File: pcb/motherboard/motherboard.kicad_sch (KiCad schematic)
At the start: 47 parts, among them J10 M20-7820646, J11 M20-7820646, J12 M20-7820646, J13 M20-7820646, J14 M20-7820646, J15 M20-7820646, J16 M20-7820646, J17 Terminal 1, J18 Terminal 2, J3 UART_USB, J4 I2C_HEADER, J6 SPI_TEST, J7 M20-7820646, J8 M20-7820646, J9 M20-7820646, SW2 GEN_MAZE, SW3 TOGGLE_MAZE, SW4 SOLVE_MAZE, U2 CH340C, U6 PCA9306D

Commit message: finished initial PCB layout for motherboard
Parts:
- removed H2: MountingHole, MountingHole:MountingHole_4.3mm_M4, symbol Mechanical:MountingHole
- removed J10, J12, J14, J16, J8: M20-7820646, KiCad:HDRV6W70P0X254_1X6_1564X250X850P, symbol KiCad:M20-7820646
- added C28, C29, C30, C31, C32: 220uF, Capacitor_SMD:CP_Elec_6.3x5.4, symbol Device:C_Polarized_Small_US
- added J19, J20, J21, J22, J23: Terminal Block, TerminalBlock_Phoenix:TerminalBlock_Phoenix_MKDS-1,5-3-5.08_1x03_P5.08mm_Horizontal, symbol Connector:Screw_Terminal_01x03
- added TP8: GND, TestPoint:TestPoint_Pad_2.0x2.0mm, symbol Connector:TestPoint
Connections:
- net +3V3: now also J19.2 (Pin_2), J20.2 (Pin_2), J21.2 (Pin_2), J22.2 (Pin_2), J23.2 (Pin_2)
- net +5V5: now also C28.1, C29.1, C30.1, C31.1, C32.1, J19.1 (Pin_1), J20.1 (Pin_1), J21.1 (Pin_1), J22.1 (Pin_1), J23.1 (Pin_1)
- net GND: now also C28.2, C29.2, C30.2, C31.2, C32.2, J19.3 (Pin_3), J20.3 (Pin_3), J21.3 (Pin_3), J22.3 (Pin_3), J23.3 (Pin_3), TP8.1

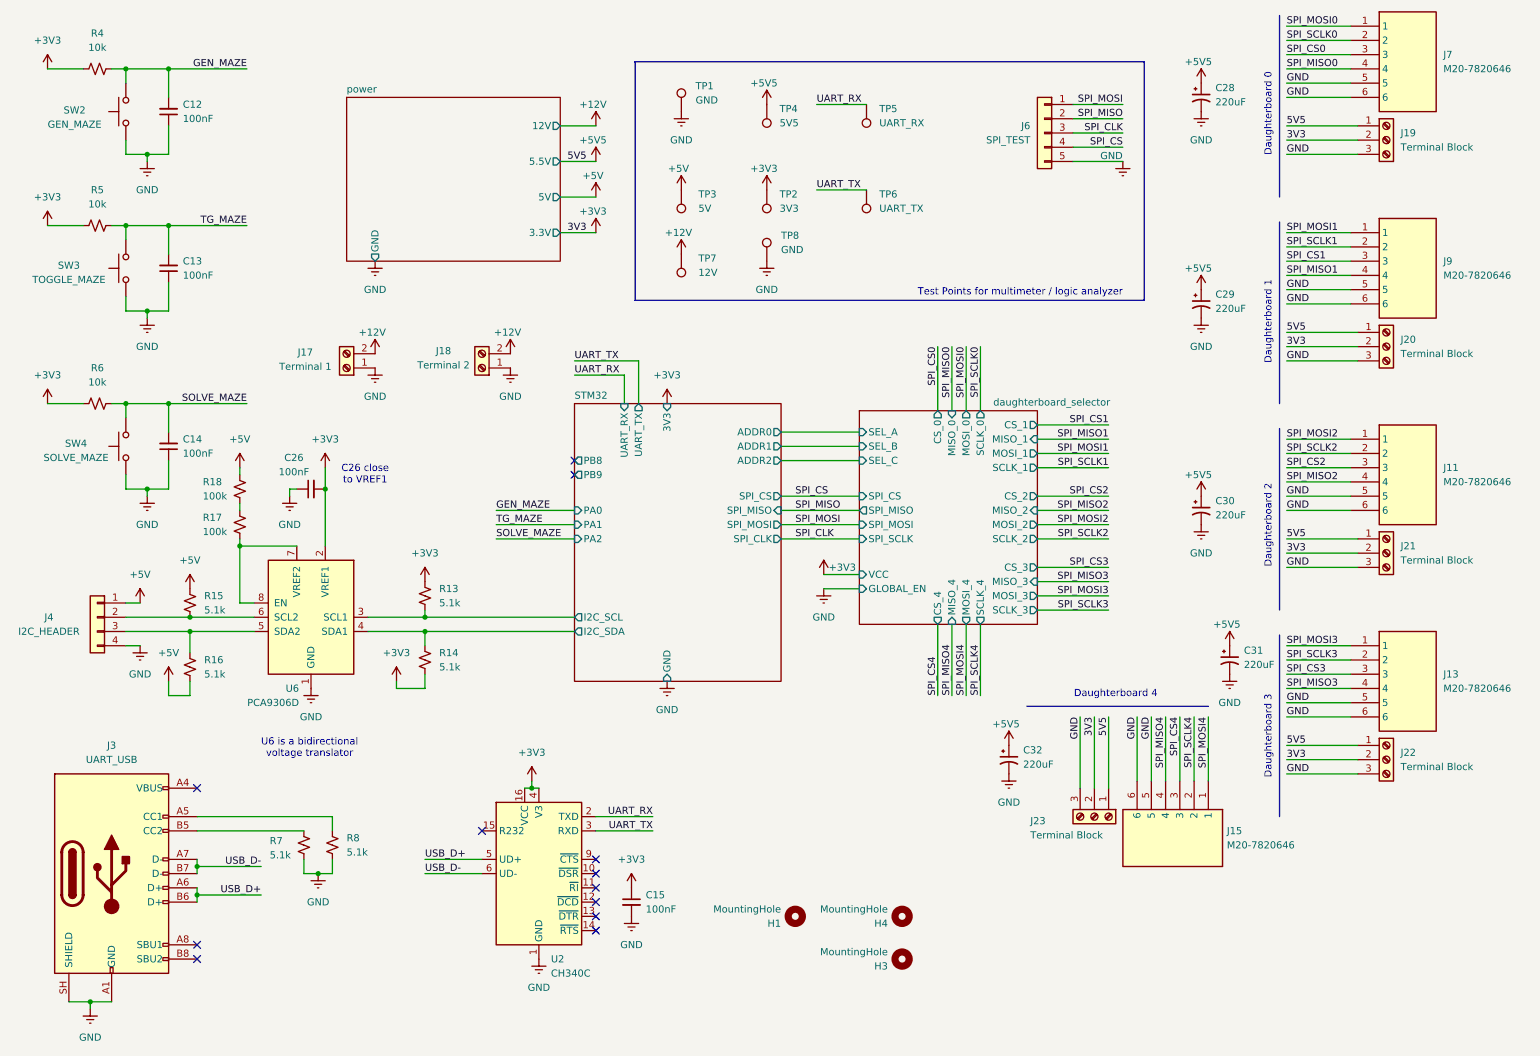
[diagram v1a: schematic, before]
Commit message: added connectors for external motors, finished most of the motherboard PCB
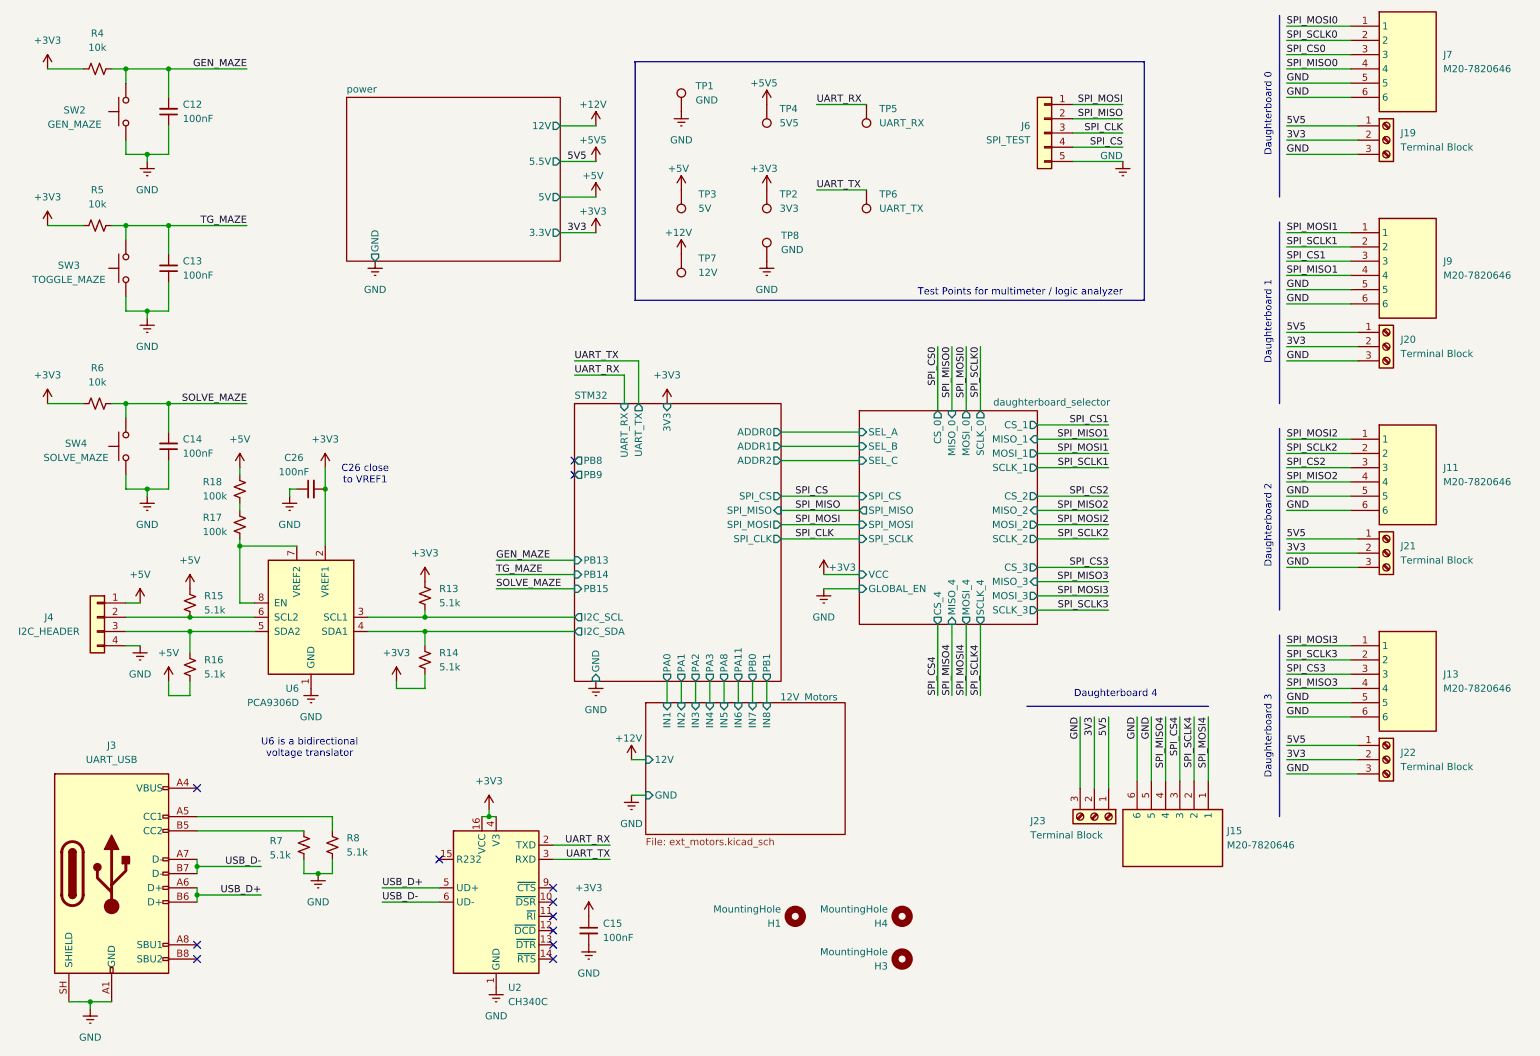
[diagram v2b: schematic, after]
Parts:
- removed C28, C29, C30, C31, C32: 220uF, Capacitor_SMD:CP_Elec_6.3x5.4, symbol Device:C_Polarized_Small_US
- removed J17: Terminal 1, TerminalBlock_Phoenix:TerminalBlock_Phoenix_MKDS-1,5-2-5.08_1x02_P5.08mm_Horizontal, symbol Connector:Screw_Terminal_01x02
- removed J18: Terminal 2, TerminalBlock_Phoenix:TerminalBlock_Phoenix_MKDS-1,5-2-5.08_1x02_P5.08mm_Horizontal, symbol Connector:Screw_Terminal_01x02
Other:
- added sheet 12V_Motors (ext_motors.kicad_sch)
- sheet STM32 ports: added PA11, PA3, PA8, PB0, PB1, PB13, PB14, PB15; removed none
- moved on the sheet: C15, U2

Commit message: Final touches for the PCB order Added MPN, Description, checked footprints and 3D models Finished the BOM
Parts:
- C12, C13, C14, C15, C26: Manufacturer_Name (none) -> YAGEO; Manufacturer_Part_Number (none) -> CC0603KRX7R9BB104
- J19, J20, J21, J22, J23: Manufacturer_Name (none) -> Phoenix Contact; Manufacturer_Part_Number (none) -> 1729021
- J3: Manufacturer_Name (none) -> HRO; Manufacturer_Part_Number (none) -> TYPE-C-31-M-12
- J4: Manufacturer_Name (none) -> Wurth Elektronik; Manufacturer_Part_Number (none) -> 61300411121
- J6: Manufacturer_Name (none) -> Wurth Elektronik; Manufacturer_Part_Number (none) -> 61300511121
- R13, R14, R15, R16, R7, R8: Manufacturer_Name (none) -> YAGEO; Manufacturer_Part_Number (none) -> RC0603FR-075K1L
- R17, R18: Manufacturer_Name (none) -> YAGEO; Manufacturer_Part_Number (none) -> RC0603FR-07100KL
- R4, R5, R6: Manufacturer_Name (none) -> YAGEO; Manufacturer_Part_Number (none) -> RC0603FR-0710KL
- SW2, SW3, SW4: Manufacturer_Name (none) -> Wurth Elektronik; Manufacturer_Part_Number (none) -> 61300211121
- U2: Manufacturer_Name (none) -> WCH; Manufacturer_Part_Number (none) -> CH340C
- U6: Manufacturer_Name (none) -> NXP; Manufacturer_Part_Number (none) -> PCA9306D

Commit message: updated MPN in BOM
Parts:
- C12, C13, C14, C15, C26: Manufacturer_Part_Number CC0603KRX7R9BB104 -> CC0603JRX7R9BB104
- J19, J20, J21, J22, J23: Manufacturer_Part_Number 1729021 -> 1729131
- J3: Manufacturer_Part_Number TYPE-C-31-M-12 -> UJ20-C-H-G-SMT-2A-P16-TR
- R13, R14, R15, R16, R7, R8: Manufacturer_Part_Number RC0603FR-075K1L -> CR0603-FX-5101ELF
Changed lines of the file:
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@@
 			)
 		)
-		(property "Manufacturer_Part_Number" "1729021"
+		(property "Manufacturer_Part_Number" "1729131"
 			(at 205.74 156.21 90)
 			(hide yes)
@@
 			)
 		)
-		(property "Manufacturer_Part_Number" "RC0603FR-075K1L"
+		(property "Manufacturer_Part_Number" "CR0603-FX-5101ELF"
 			(at 44.45 129.54 0)
 			(hide yes)
@@
 			)
 		)
-		(property "Manufacturer_Part_Number" "RC0603FR-075K1L"
+		(property "Manufacturer_Part_Number" "CR0603-FX-5101ELF"
 			(at 86.36 128.27 0)
 			(hide yes)
@@
 			)
 		)
-		(property "Manufacturer_Part_Number" "1729021"
+		(property "Manufacturer_Part_Number" "1729131"
 			(at 257.81 146.05 0)
 			(hide yes)
@@
 			)
 		)
-		(property "Manufacturer_Part_Number" "1729021"
+		(property "Manufacturer_Part_Number" "1729131"
 			(at 257.81 109.22 0)
 			(hide yes)
@@
 			)
 		)
-		(property "Manufacturer_Part_Number" "TYPE-C-31-M-12"
+		(property "Manufacturer_Part_Number" " UJ20-C-H-G-SMT-2A-P16-TR"
 			(at 30.48 166.37 0)
 			(hide yes)
@@
 			)
 		)
-		(property "Manufacturer_Part_Number" "CC0603KRX7R9BB104"
+		(property "Manufacturer_Part_Number" "CC0603JRX7R9BB104"
 			(at 40.64 30.48 0)
 			(hide yes)
@@
 			)
 		)
-		(property "Manufacturer_Part_Number" "RC0603FR-075K1L"
+		(property "Manufacturer_Part_Number" "CR0603-FX-5101ELF"
 			(at 44.45 118.11 0)
 			(hide yes)
@@
 			)
 		)
-		(property "Manufacturer_Part_Number" "RC0603FR-075K1L"
+		(property "Manufacturer_Part_Number" "CR0603-FX-5101ELF"
 			(at 69.85 161.29 0)
 			(hide yes)
@@
 			)
 		)
-		(property "Manufacturer_Part_Number" "1729021"
+		(property "Manufacturer_Part_Number" "1729131"
 			(at 257.81 72.39 0)
 			(hide yes)
@@
 			)
 		)
-		(property "Manufacturer_Part_Number" "1729021"
+		(property "Manufacturer_Part_Number" "1729131"
 			(at 257.81 35.56 0)
 			(hide yes)
@@
 			)
 		)
-		(property "Manufacturer_Part_Number" "RC0603FR-075K1L"
+		(property "Manufacturer_Part_Number" "CR0603-FX-5101ELF"
 			(at 64.77 161.29 0)
 			(hide yes)
@@
 			)
 		)
-		(property "Manufacturer_Part_Number" "CC0603KRX7R9BB104"
+		(property "Manufacturer_Part_Number" "CC0603JRX7R9BB104"
 			(at 40.64 90.17 0)
 			(hide yes)
@@
 			)
 		)
-		(property "Manufacturer_Part_Number" "CC0603KRX7R9BB104"
+		(property "Manufacturer_Part_Number" "CC0603JRX7R9BB104"
 			(at 40.64 58.42 0)
 			(hide yes)
@@
 			)
 		)
-		(property "Manufacturer_Part_Number" "CC0603KRX7R9BB104"
+		(property "Manufacturer_Part_Number" "CC0603JRX7R9BB104"
 			(at 115.57 176.53 0)
 			(hide yes)
@@
 			)
 		)
-		(property "Manufacturer_Part_Number" "RC0603FR-075K1L"
+		(property "Manufacturer_Part_Number" "CR0603-FX-5101ELF"
 			(at 86.36 116.84 0)
 			(hide yes)
@@
 			)
 		)
-		(property "Manufacturer_Part_Number" "CC0603KRX7R9BB104"
+		(property "Manufacturer_Part_Number" "CC0603JRX7R9BB104"
 			(at 66.04 97.79 90)
 			(hide yes)

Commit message: modified MPN
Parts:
- U6: value PCA9306D -> PCA9306DCUR; footprint Package_SO:SO-8_3.9x4.9mm_P1.27mm -> Package_SON:X2SON-8_1.4x1mm_P0.35mm; Manufacturer_Part_Number PCA9306D -> PCA9306DCUR
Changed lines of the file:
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@@
 			)
 		)
-		(property "Value" "PCA9306D"
+		(property "Value" "PCA9306DCUR"
 			(at 63.8967 135.89 0)
 			(show_name no)
@@
 			)
 		)
-		(property "Footprint" "Package_SO:SO-8_3.9x4.9mm_P1.27mm"
+		(property "Footprint" "Package_SON:X2SON-8_1.4x1mm_P0.35mm"
 			(at 66.04 132.08 0)
 			(hide yes)
@@
 			)
 		)
-		(property "Manufacturer_Part_Number" "PCA9306D"
+		(property "Manufacturer_Part_Number" "PCA9306DCUR"
 			(at 66.04 120.65 0)
 			(hide yes)
